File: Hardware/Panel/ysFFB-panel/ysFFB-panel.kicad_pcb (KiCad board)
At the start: 2 copper layers, 200 x 200 mm, 26 parts

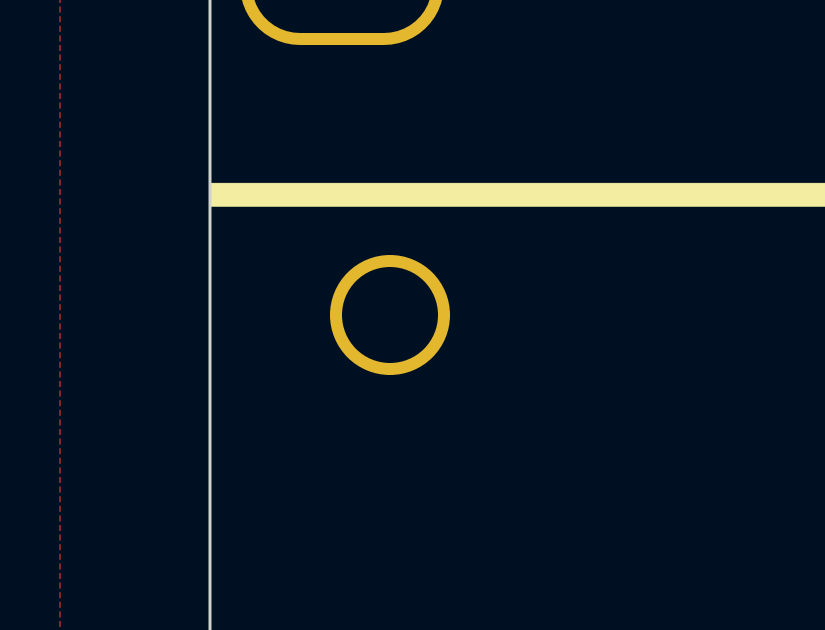
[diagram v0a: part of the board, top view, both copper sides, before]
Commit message: Pre fab tweaks, new Gerbers, correct alignment and make PCB dimensions symmetric in module
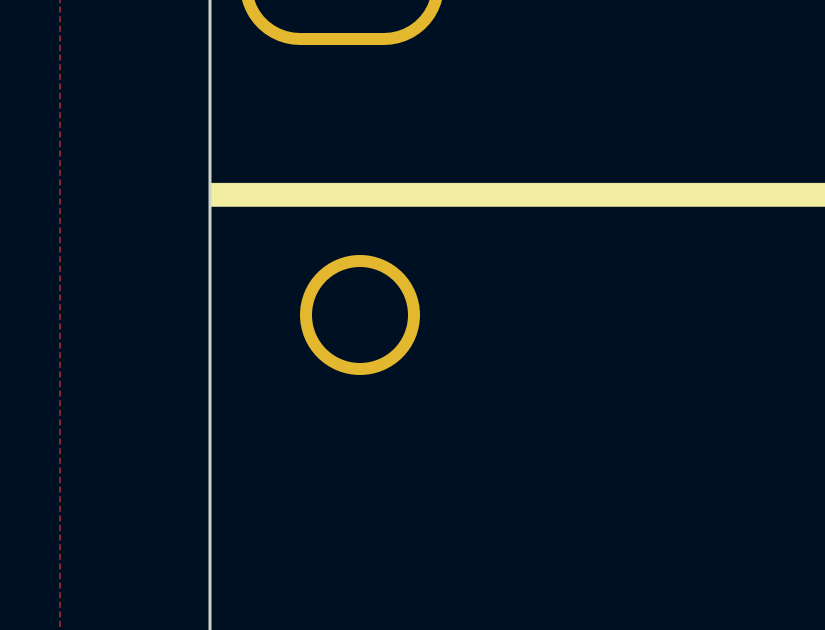
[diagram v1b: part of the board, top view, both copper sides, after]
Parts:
- H10, H13, H16, H19, H5: value Jack_Hole_NPTH -> Jack_Hole
- H6, H7: value Mounting_Hole_NPTH -> Mounting_Hole
- moved H6 1.00 mm to (5.00, 14.0)
